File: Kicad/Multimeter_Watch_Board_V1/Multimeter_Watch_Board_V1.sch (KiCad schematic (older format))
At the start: 14 parts, among them J1 AudioJack3_Ground_renamedPins, J2 AudioJack3_Ground_renamedPins, J3 AudioJack3_Ground_renamedPins

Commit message: fix shunt resistor
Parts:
- removed R6: R_Shunt, Resistor_SMD:R_2512_6332Metric_Pad1.52x3.35mm_HandSolder, symbol Device:R_Shunt
- added R6: R_shunt, symbol Device:R
- added U1: PCF85163-SO08, Package_SO:SOIC-8-1EP_3.9x4.9mm_P1.27mm_EP2.29x3mm, symbol Multimeter_Watch_Custom_Symbols:PCF85163-SO08
- added Y1: 32kHz, Crystal:Crystal_SMD_3215-2Pin_3.2x1.5mm, symbol Device:Crystal
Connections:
- wire segments 30 -> 34
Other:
- moved on the sheet: J1, J2, J3, R1, R10, R2, R3, R4, R5, R7, R8, R9

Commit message: i2c / rtc
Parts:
- added R11, R12: R, symbol Device:R
- R6: footprint (none) -> Resistor_SMD:R_2512_6332Metric_Pad1.52x3.35mm_HandSolder
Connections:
- net labels added: NC, Nk, SCL, SDA, VCC
- wire segments 34 -> 67
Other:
- note added: "I2C/RTC\n"
- moved on the sheet: U1, Y1
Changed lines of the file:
@@
 Wire Wire Line
 	2350 1050 2400 1050
-Text Label 1300 1400 0    47   ~ 0
+Text Label 1550 1400 0    47   ~ 0
 PD3
-Text Label 1700 1400 0    47   ~ 0
+Text Label 1950 1400 0    47   ~ 0
 PD2
-Text Label 2100 1400 0    47   ~ 0
+Text Label 2350 1400 0    47   ~ 0
 ADC11
-Text Label 900  1400 0    47   ~ 0
-ADC10
 Text Label 2600 2100 0    47   ~ 0
 ADC2
@@
 L Device:Crystal Y1
 U 1 1 5F21906D
-P 5100 1250
-F 0 "Y1" V 5054 1381 50  0000 L CNN
-F 1 "32kHz" V 5145 1381 50  0000 L CNN
-F 2 "Crystal:Crystal_SMD_3215-2Pin_3.2x1.5mm" H 5100 1250 50  0001 C CNN
-F 3 "~" H 5100 1250 50  0001 C CNN
-	1    5100 1250
-	0    1    1    0
+P 4700 850
+F 0 "Y1" H 4700 1118 50  0000 C CNN
+F 1 "32kHz" H 4700 1027 50  0000 C CNN
+F 2 "Crystal:Crystal_SMD_3215-2Pin_3.2x1.5mm" H 4700 850 50  0001 C CNN
+F 3 "~" H 4700 850 50  0001 C CNN
+	1    4700 850
+	1    0    0    -1
 $EndComp
 $Comp
 L Multimeter_Watch_Custom_Symbols:PCF85163-SO08 U1
 U 1 1 5F21CC1C
-P 6250 1300
-F 0 "U1" H 6250 1659 47  0000 C CNN
-F 1 "PCF85163-SO08" H 6250 1572 47  0000 C CNN
-F 2 "Package_SO:SOIC-8-1EP_3.9x4.9mm_P1.27mm_EP2.29x3mm" H 6150 1250 47  0001 C CNN
-F 3 "" H 6150 1250 47  0001 C CNN
-	1    6250 1300
+P 5400 1250
+F 0 "U1" H 5400 1609 47  0000 C CNN
+F 1 "PCF85163-SO08" H 5400 1522 47  0000 C CNN
+F 2 "Package_SO:SOIC-8-1EP_3.9x4.9mm_P1.27mm_EP2.29x3mm" H 5300 1200 47  0001 C CNN
+F 3 "" H 5300 1200 47  0001 C CNN
+	1    5400 1250
 	1    0    0    -1
 $EndComp
@@
 F 0 "R6" V 2593 2200 50  0000 C CNN
 F 1 "R_shunt" V 2684 2200 50  0000 C CNN
-F 2 "" V 2730 2200 50  0001 C CNN
+F 2 "Resistor_SMD:R_2512_6332Metric_Pad1.52x3.35mm_HandSolder" V 2730 2200 50  0001 C CNN
 F 3 "~" H 2800 2200 50  0001 C CNN
 	1    2800 2200
@@
 	2600 2200 2600 2100
 Connection ~ 2600 2200
+Wire Wire Line
+	4950 1100 4850 1100
+Wire Wire Line
+	4850 1100 4850 850
+Wire Wire Line
+	4550 850  4550 1200
+Wire Wire Line
+	4550 1200 4950 1200
+Wire Wire Line
+	4950 1300 4550 1300
+Text Label 4550 1300 0    47   ~ 0
+Nk
+Text Label 900  1400 0    47   ~ 0
+ADC10
+Wire Wire Line
+	5850 1200 6000 1200
+Text Label 6000 1200 0    47   ~ 0
+NC
+Wire Wire Line
+	5850 1100 6300 1100
+$Comp
+L Device:R R11
+U 1 1 5F234AFA
+P 6300 1250
+F 0 "R11" H 6370 1296 50  0000 L CNN
+F 1 "R" H 6370 1205 50  0000 L CNN
+F 2 "" V 6230 1250 50  0001 C CNN
+F 3 "~" H 6300 1250 50  0001 C CNN
+	1    6300 1250
+	1    0    0    -1
+$EndComp
+Connection ~ 6300 1100
+Wire Wire Line
+	6300 1100 6550 1100
+$Comp
+L Device:R R12
+U 1 1 5F2353C3
+P 6550 1250
+F 0 "R12" H 6620 1296 50  0000 L CNN
+F 1 "R" H 6620 1205 50  0000 L CNN
+F 2 "" V 6480 1250 50  0001 C CNN
+F 3 "~" H 6550 1250 50  0001 C CNN
+	1    6550 1250
+	1    0    0    -1
+$EndComp
+Connection ~ 6550 1100
+Wire Wire Line
+	5850 1300 6150 1300
+Wire Wire Line
+	6150 1300 6150 1500
+Wire Wire Line
+	6150 1500 6300 1500
+Wire Wire Line
+	6550 1100 6800 1100
+Wire Wire Line
+	5850 1400 6050 1400
+Wire Wire Line
+	6050 1400 6050 1600
+Wire Wire Line
+	6050 1600 6550 1600
+Wire Wire Line
+	6300 1400 6300 1500
+Connection ~ 6300 1500
+Wire Wire Line
+	6300 1500 6800 1500
+Wire Wire Line
+	6550 1400 6550 1600
+Connection ~ 6550 1600
+Wire Wire Line
+	6550 1600 6800 1600
+Text Label 6800 1500 0    47   ~ 0
+SCL
+Text Label 6800 1600 0    47   ~ 0
+SDA
+Text Label 6800 1100 0    47   ~ 0
+VCC
+Wire Wire Line
+	7000 3450 7000 3200
+Wire Wire Line
+	7000 3200 6800 3200
+Wire Wire Line
+	7100 3450 7100 3100
+Wire Wire Line
+	7100 3100 6800 3100
+Wire Wire Line
+	7200 3450 7200 3000
+Wire Wire Line
+	7200 3000 6800 3000
+Wire Wire Line
+	7600 3450 7600 3300
+Wire Wire Line
+	7600 3300 7700 3300
+Wire Wire Line
+	7500 3450 7500 3200
+Wire Wire Line
+	7500 3200 7700 3200
+Wire Wire Line
+	7400 3450 7400 3100
+Wire Wire Line
+	7400 3100 7700 3100
+Wire Wire Line
+	7300 3450 7300 3000
+Wire Wire Line
+	7300 3000 7700 3000
+Text Label 7700 3100 0    47   ~ 0
+SCL
+Text Label 7700 3000 0    47   ~ 0
+SDA
+Text Notes 5400 750  0    118  ~ 0
+I2C/RTC\n
 $EndSCHEMATC

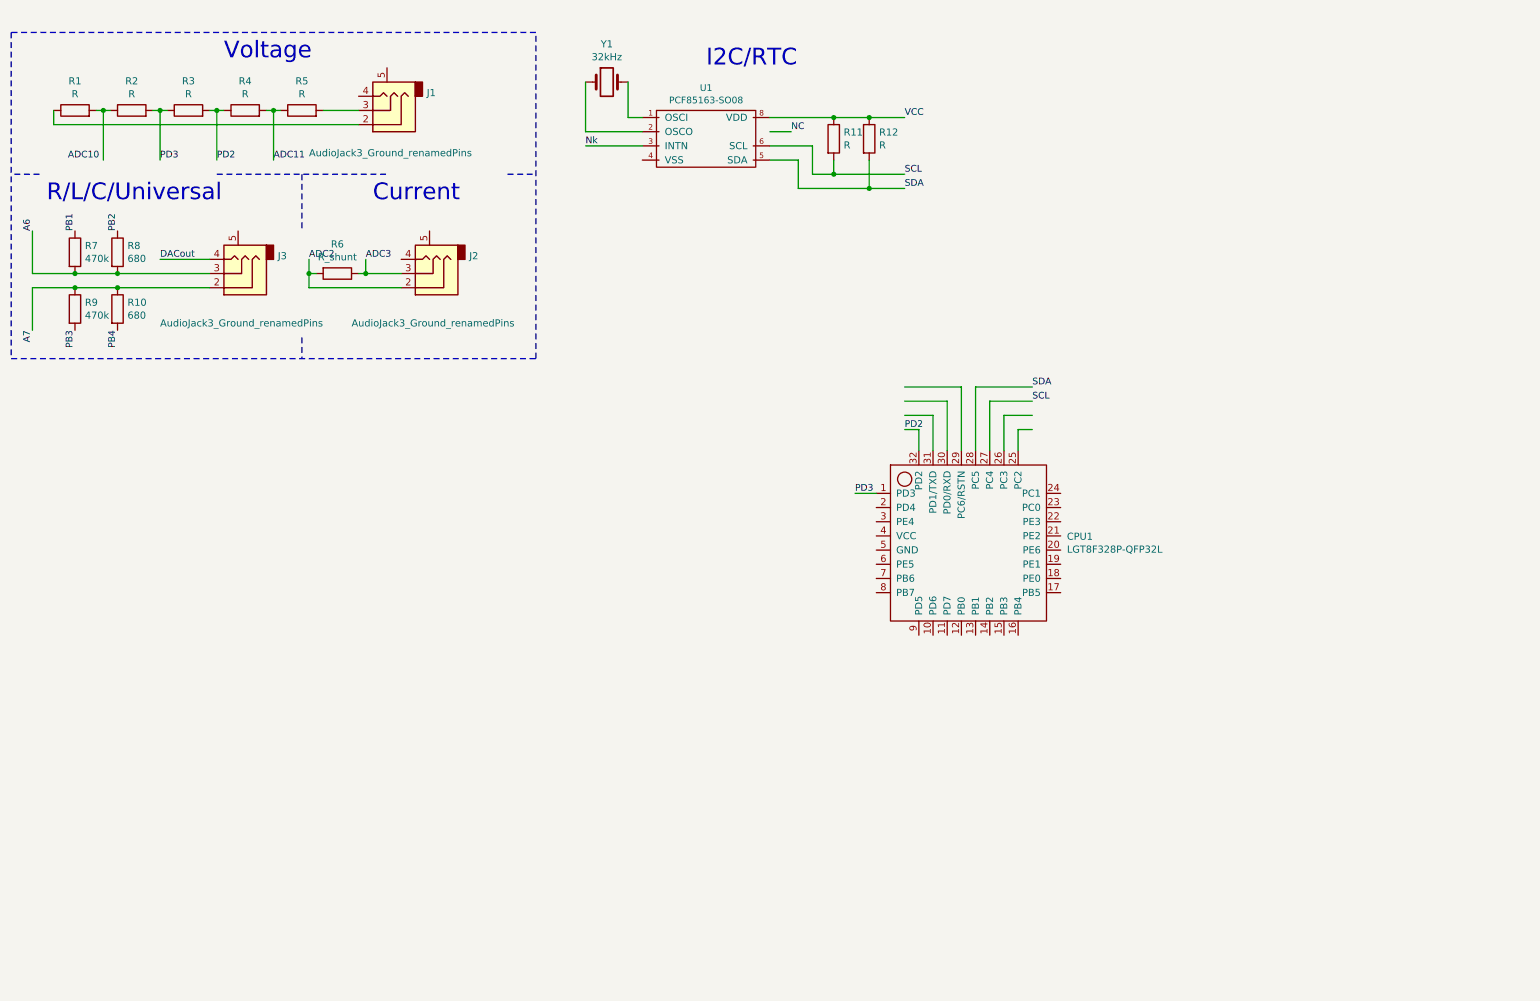
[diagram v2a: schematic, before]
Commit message: proc. board schematic (mostly) done, fist female connector version
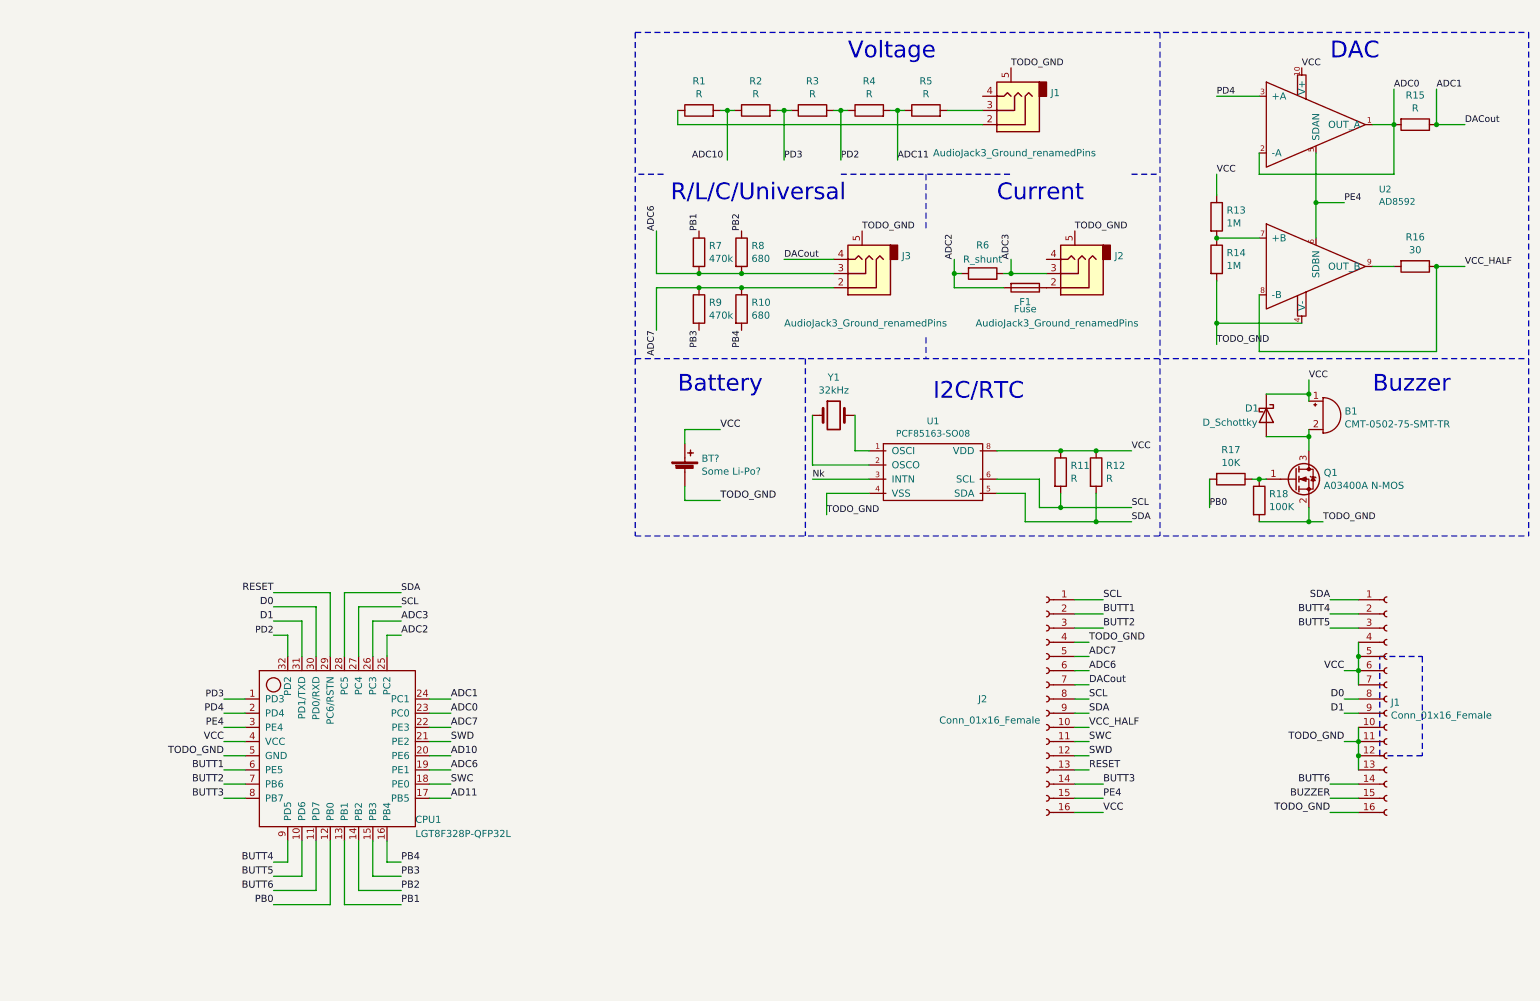
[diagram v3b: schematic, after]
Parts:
- added B1: CMT-0502-75-SMT-TR, symbol Device:Buzzer
- added BT?: Some Li-Po?, symbol Device:Battery_Cell
- added D1: D_Schottky, symbol Device:D_Schottky
- added F1: Fuse, Fuse:Fuse_0805_2012Metric_Pad1.15x1.40mm_HandSolder, symbol Device:Fuse
- added J1, J2: Conn_01x16_Female, Connector_PinSocket_2.54mm:PinSocket_1x16_P2.54mm_Vertical, symbol Connector:Conn_01x16_Female
- added Q1: A03400A N-MOS, Package_TO_SOT_SMD:SOT-23, symbol Transistor_FET:2N7002E
- added R13, R14: 1M, symbol Device:R
- added R15: R, Resistor_SMD:R_2512_6332Metric_Pad1.52x3.35mm_HandSolder, symbol Device:R
- added R16: 30, Resistor_SMD:R_2512_6332Metric_Pad1.52x3.35mm_HandSolder, symbol Device:R
- added R17: 10K, symbol Device:R
- added R18: 100K, symbol Device:R
- added U2: AD8592, symbol Multimeter_Watch_Custom_Symbols:AD8592
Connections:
- net labels added: AD10, AD11, ADC0, ADC1, ADC6, ADC7, BUTT1, BUTT2, BUTT3, BUTT4, BUTT5, BUTT6, BUZZER, D0, D1, PB0, PD4, PE4, RESET, SWC, SWD, TODO_GND, VCC_HALF
- net labels removed: A6, A7, NC
- wire segments 67 -> 168
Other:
- note added: "Battery"
- note added: "Buzzer\n"
- note added: "DAC"
- moved on the sheet: CPU1, J1, J2, J3, R1, R10, R11, R12, R2, R3, R4, R5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

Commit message: start work on pcb layout
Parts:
- removed B1: CMT-0502-75-SMT-TR, symbol Device:Buzzer
- removed D1: D_Schottky, symbol Device:D_Schottky
- removed Q1: A03400A N-MOS, Package_TO_SOT_SMD:SOT-23, symbol Transistor_FET:2N7002E
- removed R17: 10K, symbol Device:R
- removed R18: 100K, symbol Device:R
- added C1, C2, C3: 100n, Capacitor_SMD:C_0603_1608Metric_Pad1.05x0.95mm_HandSolder, symbol Device:C_Small
- BT1: renamed from BT?; footprint (none) -> Connector_Molex:Molex_PicoBlade_53047-0210_1x02_P1.25mm_Vertical
- R11, R12, R13, R14: footprint (none) -> Resistor_SMD:R_0603_1608Metric_Pad1.05x0.95mm_HandSolder
- U2: footprint (none) -> Package_SO:MSOP-10_3x3mm_P0.5mm
- renumbered J2 to J4, J1 to J5
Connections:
- net BUZZER is gone; now on net PB0: J5.15 (Pin_15)
- net ADC0: no longer U2.2 (-A)
- net ADC1: now also U2.2 (-A)
- net TODO_GND: no longer BT1.2 (-), CPU1.5 (GND), J1.5, J2.5, J3.5, J5.10 (Pin_10), J5.11 (Pin_11), J5.12 (Pin_12), J5.13 (Pin_13), J5.16 (Pin_16), R14.2, U1.4 (VSS), U2.4 (V-)
- net VCC: now also C1.2, C2.1, C3.1
- net Nk: no longer names the net of U1.3 (INTN)
- new net GND: BT1.2 (-), C1.1, C2.2, C3.2, CPU1.5 (GND), J5.10 (Pin_10), J5.11 (Pin_11), J5.12 (Pin_12), J5.13 (Pin_13), J5.16 (Pin_16), R14.2, U1.4 (VSS), U2.4 (V-)
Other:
- note added: "BUZZER"
- note added: "Charger/Comm shield outline"
- note added: "Has been moved to DisplayBoard"
- note removed: "Buzzer\n"
- moved on the sheet: CPU1, J4, J5, R11, R12, U1, Y1
